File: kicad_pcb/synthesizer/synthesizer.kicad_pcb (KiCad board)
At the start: 2 copper layers, 122.2 x 82 mm, 39 parts, among them J1 RJ45, J5 CONSMA006.062-G, Q1 BCW31_

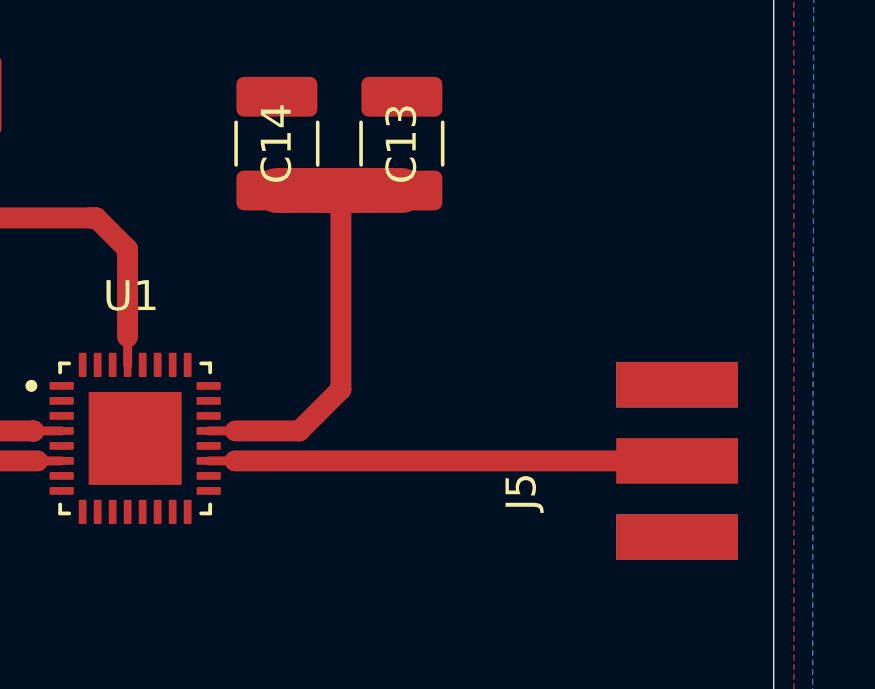
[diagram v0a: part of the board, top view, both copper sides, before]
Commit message: Agregada LineaPCB
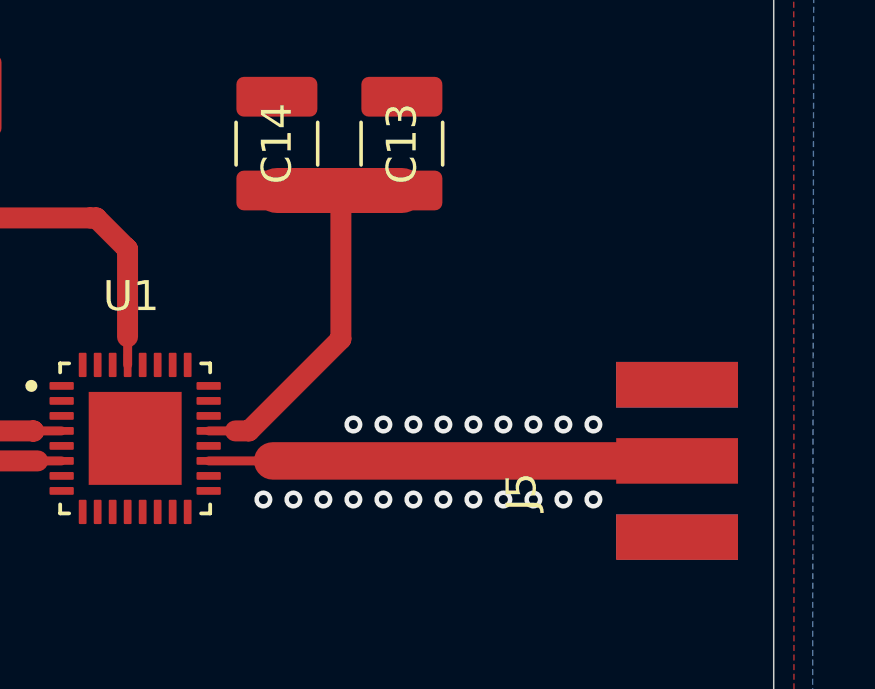
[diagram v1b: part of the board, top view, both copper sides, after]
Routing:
- net +5V: track 127.2 -> 126.3 mm
- net GND: vias 0 -> 21
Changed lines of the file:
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@@
 			(keep_text_aligned yes)
 		)
-		(gr_text "122.2248"
+		(gr_text "122,2248"
 			(at 153.8986 57.9558 0)
 			(layer "Dwgs.User")
@@
 			(keep_text_aligned yes)
 		)
-		(gr_text "82.042"
+		(gr_text "82,042"
 			(at 86.607 105.283 90)
 			(layer "Dwgs.User")
@@
 		(net 2)
 	)
+	(via
+		(at 203 105.5)
+		(size 0.6)
+		(drill 0.3)
+		(layers "F.Cu" "B.Cu")
+		(free yes)
+		(net 2)
+	)
+	(via
+		(at 204 103)
+		(size 0.6)
+		(drill 0.3)
+		(layers "F.Cu" "B.Cu")
+		(free yes)
+		(net 2)
+	)
+	(via
+		(at 209 105.5)
+		(size 0.6)
+		(drill 0.3)
+		(layers "F.Cu" "B.Cu")
+		(free yes)
+		(net 2)
+	)
+	(via
+		(at 209 103)
+		(size 0.6)
+		(drill 0.3)
+		(layers "F.Cu" "B.Cu")
+		(free yes)
+		(net 2)
+	)
+	(via
+		(at 206 103)
+		(size 0.6)
+		(drill 0.3)
+		(layers "F.Cu" "B.Cu")
+		(free yes)
+		(net 2)
+	)
+	(via
+		(at 207 105.5)
+		(size 0.6)
+		(drill 0.3)
+		(layers "F.Cu" "B.Cu")
+		(free yes)
+		(net 2)
+	)
+	(via
+		(at 199 105.5)
+		(size 0.6)
+		(drill 0.3)
+		(layers "F.Cu" "B.Cu")
+		(free yes)
+		(net 2)
+	)
+	(via
+		(at 202 103)
+		(size 0.6)
+		(drill 0.3)
+		(layers "F.Cu" "B.Cu")
+		(free yes)
+		(net 2)
+	)
+	(via
+		(at 198 105.5)
+		(size 0.6)
+		(drill 0.3)
+		(layers "F.Cu" "B.Cu")
+		(free yes)
+		(net 2)
+	)
+	(via
+		(at 208 103)
+		(size 0.6)
+		(drill 0.3)
+		(layers "F.Cu" "B.Cu")
+		(free yes)
+		(net 2)
+	)
+	(via
+		(at 201 103)
+		(size 0.6)
+		(drill 0.3)
+		(layers "F.Cu" "B.Cu")
+		(free yes)
+		(net 2)
+	)
+	(via
+		(at 203 103)
+		(size 0.6)
+		(drill 0.3)
+		(layers "F.Cu" "B.Cu")
+		(free yes)
+		(net 2)
+	)
+	(via
+		(at 201 105.5)
+		(size 0.6)
+		(drill 0.3)
+		(layers "F.Cu" "B.Cu")
+		(free yes)
+		(net 2)
+	)
+	(via
+		(at 202 105.5)
+		(size 0.6)
+		(drill 0.3)
+		(layers "F.Cu" "B.Cu")
+		(free yes)
+		(net 2)
+	)
+	(via
+		(at 205 103)
+		(size 0.6)
+		(drill 0.3)
+		(layers "F.Cu" "B.Cu")
+		(free yes)
+		(net 2)
+	)
+	(via
+		(at 208 105.5)
+		(size 0.6)
+		(drill 0.3)
+		(layers "F.Cu" "B.Cu")
+		(free yes)
+		(net 2)
+	)
+	(via
+		(at 207 103)
+		(size 0.6)
+		(drill 0.3)
+		(layers "F.Cu" "B.Cu")
+		(free yes)
+		(net 2)
+	)
+	(via
+		(at 200 105.5)
+		(size 0.6)
+		(drill 0.3)
+		(layers "F.Cu" "B.Cu")
+		(free yes)
+		(net 2)
+	)
+	(via
+		(at 205 105.5)
+		(size 0.6)
+		(drill 0.3)
+		(layers "F.Cu" "B.Cu")
+		(free yes)
+		(net 2)
+	)
+	(via
+		(at 206 105.5)
+		(size 0.6)
+		(drill 0.3)
+		(layers "F.Cu" "B.Cu")
+		(free yes)
+		(net 2)
+	)
+	(via
+		(at 204 105.5)
+		(size 0.6)
+		(drill 0.3)
+		(layers "F.Cu" "B.Cu")
+		(free yes)
+		(net 2)
+	)
 	(segment
 		(start 190.4779 104.2129)
@@
 	)
 	(segment
+		(start 197.0659 103.2129)
+		(end 197.52 103.2129)
+		(width 0.700001)
+		(layer "F.Cu")
+		(net 3)
+	)
+	(segment
+		(start 197.52 103.2129)
+		(end 200.5838 100.1491)
+		(width 0.700001)
+		(layer "F.Cu")
+		(net 3)
+	)
+	(segment
 		(start 185.7502 114.9604)
 		(end 178.689 114.9604)
@@
 		(end 155.6258 104.9274)
 		(width 0.399999)
-		(layer "F.Cu")
-		(net 3)
-	)
-	(segment
-		(start 200.5838 101.8286)
-		(end 200.5838 95.1992)
-		(width 0.700001)
 		(layer "F.Cu")
 		(net 3)
@@
 	)
 	(segment
-		(start 197.0659 103.2129)
-		(end 199.1995 103.2129)
-		(width 0.700001)
-		(layer "F.Cu")
-		(net 3)
-	)
-	(segment
 		(start 137.9982 108.7751)
 		(end 132.2629 108.7751)
@@
 	)
 	(segment
-		(start 199.1995 103.2129)
-		(end 200.5838 101.8286)
-		(width 0.700001)
-		(layer "F.Cu")
-		(net 3)
-	)
-	(segment
 		(start 128.6256 112.4124)
 		(end 128.3556 112.4124)
 		(width 2.000001)
+		(layer "F.Cu")
+		(net 3)
+	)
+	(segment
+		(start 200.5838 100.1491)
+		(end 200.5838 95.1992)
+		(width 0.700001)
 		(layer "F.Cu")
 		(net 3)
@@
 	)
 	(segment
-		(start 197.0499 104.2129)
+		(start 198.31 104.2129)
+		(end 196.1758 104.2129)
+		(width 0.299999)
+		(layer "F.Cu")
+		(net 19)
+	)
+	(segment
+		(start 198.31 104.2129)
 		(end 211.7902 104.2129)
-		(width 0.700001)
-		(layer "F.Cu")
-		(net 19)
-	)
-	(segment
-		(start 196.1758 104.2129)
-		(end 197.0499 104.2129)
-		(width 0.299999)
+		(width 1.25)
 		(layer "F.Cu")
 		(net 19)
@@
 		(net_name "GND")
 		(layer "F.Cu")
-		(hatch edge 0.5)
-		(connect_pads
-			(clearance 0.5)
+		(hatch edge 0.2)
+		(connect_pads yes
+			(clearance 0.2)
 		)
 		(min_thickness 0.25)

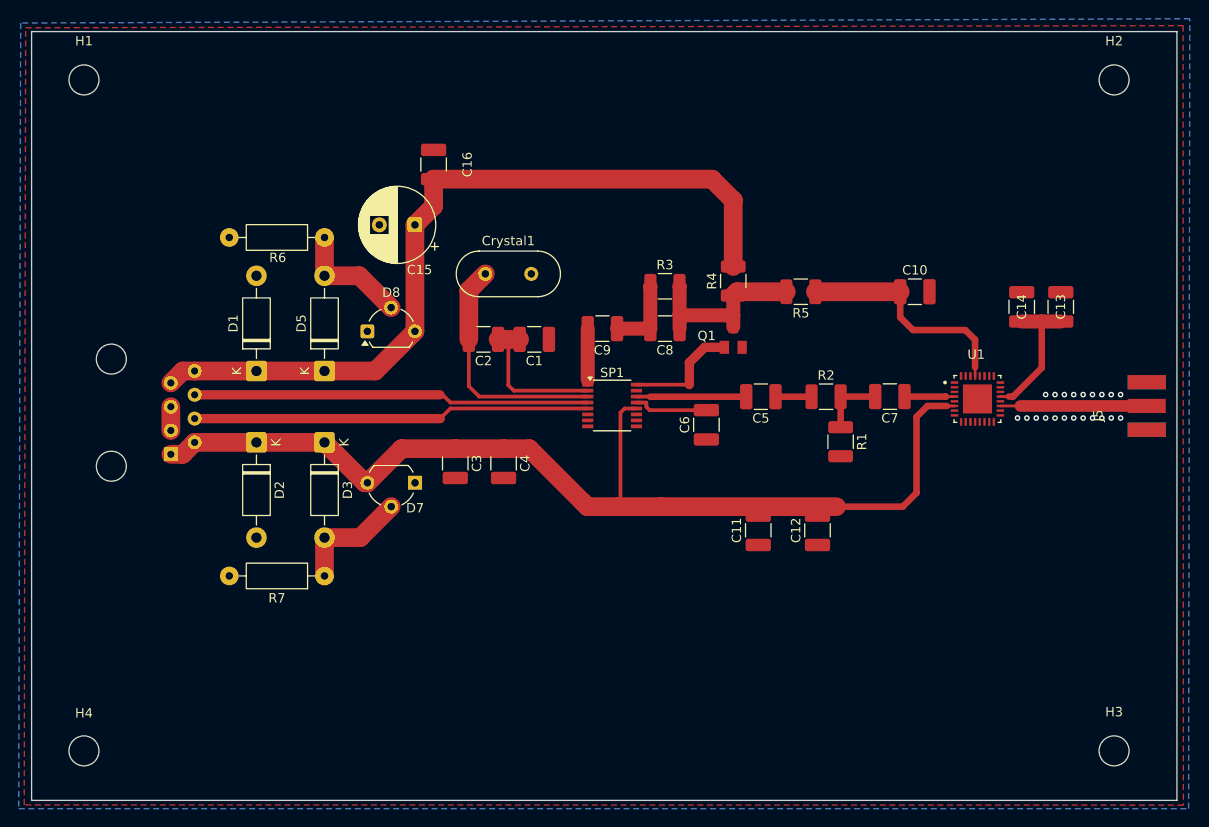
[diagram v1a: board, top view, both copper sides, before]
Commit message: modificación de pcb y esquema
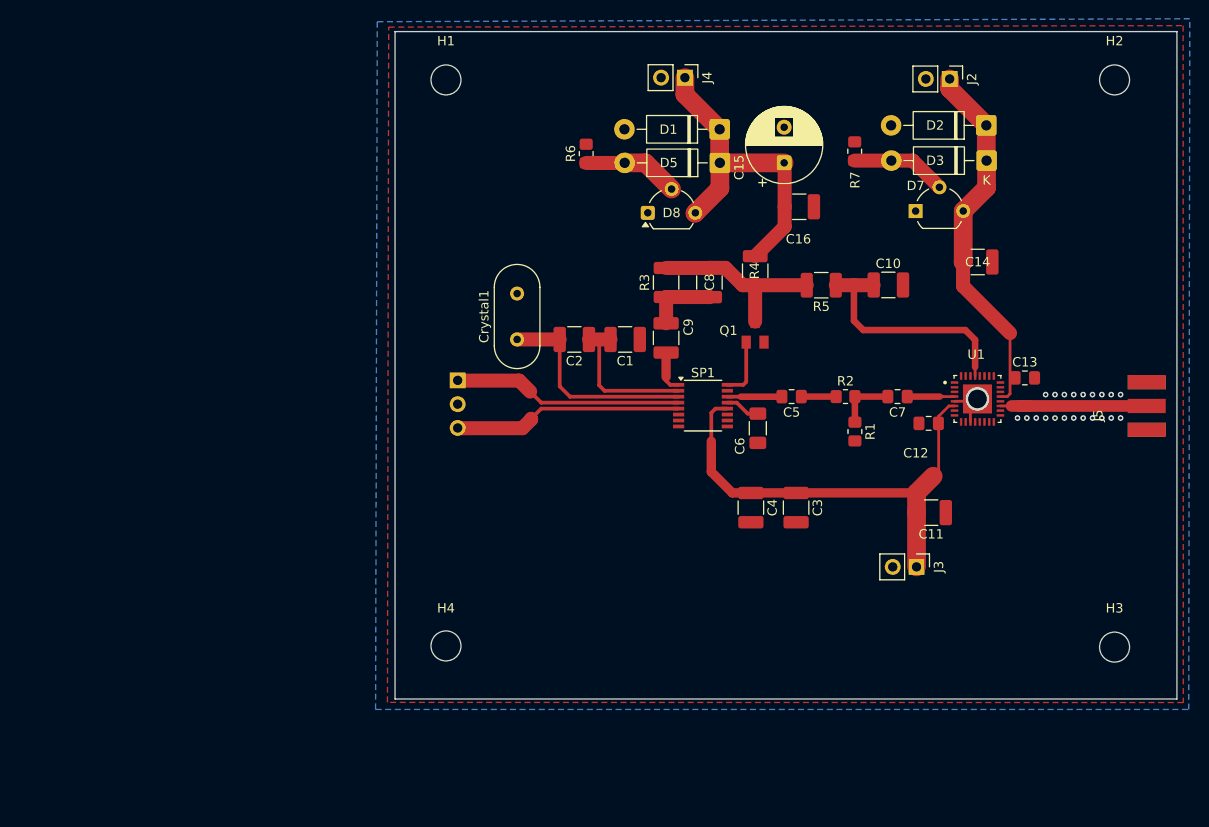
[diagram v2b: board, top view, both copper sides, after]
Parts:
- added J2: Fuente5V, Connector_PinHeader_2.54mm:PinHeader_1x02_P2.54mm_Vertical, F.Cu at (190.8, 69.3)
- added J3: Fuente5V, Connector_PinHeader_2.54mm:PinHeader_1x02_P2.54mm_Vertical, F.Cu at (187.2, 121.4)
- added J4: Fuente12V, Connector_PinHeader_2.54mm:PinHeader_1x02_P2.54mm_Vertical, F.Cu at (162.5, 69.2)
- C12, C13, C5, C7: footprint Capacitor_SMD:C_1210_3225Metric_Pad1.33x2.70mm_HandSolder -> Capacitor_SMD:C_0805_2012Metric_Pad1.18x1.45mm_HandSolder
- C6: footprint Capacitor_SMD:C_1210_3225Metric_Pad1.33x2.70mm_HandSolder -> Capacitor_SMD:C_1206_3216Metric_Pad1.33x1.80mm_HandSolder
- J1: value RJ45 -> SCL_GND_SCA; footprint Connector_RJ:RJ45_Amphenol_54602-x08_Horizontal -> Connector_PinHeader_2.54mm:PinHeader_1x03_P2.54mm_Vertical
- R1, R2: footprint Resistor_SMD:R_1210_3225Metric_Pad1.30x2.65mm_HandSolder -> Resistor_SMD:R_0805_2012Metric_Pad1.20x1.40mm_HandSolder
- R6, R7: footprint Resistor_THT:R_Axial_DIN0207_L6.3mm_D2.5mm_P10.16mm_Horizontal -> Resistor_SMD:R_0805_2012Metric_Pad1.20x1.40mm_HandSolder
- moved D2 84.9 mm to (194.7, 74.3), turned to 180 degrees
- moved D3 76.8 mm to (194.7, 78.0), turned to 180 degrees
- moved R7 72.5 mm to (180.6, 77.0), turned to 90 degrees
- moved D7 60.8 mm to (187.1, 83.4), turned to 0 degrees
- moved D1 55.8 mm to (166.2, 74.7), turned to 180 degrees
- moved D5 47.7 mm to (166.2, 78.3), turned to 180 degrees
- moved H4 40.2 mm to (137.0, 129.9)
- moved C15 40.0 mm to (173.1, 78.3), turned to 90 degrees
- moved C16 39.3 mm to (174.7, 83.0), turned to 0 degrees
- moved H1 38.6 mm to (137.0, 69.4)
- moved C3 36.7 mm to (174.4, 115.1)
- moved D8 32.5 mm to (158.5, 83.6)
- moved J1 31.6 mm to (138.3, 101.5), turned to 180 degrees
- moved R6 29.3 mm to (152.0, 77.3), turned to 90 degrees
- moved C4 26.8 mm to (169.5, 115.1)
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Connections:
- J1 pad 1: +5V -> Net-(J1-Pin_1)
- J1 pad 2: +5V -> GND
- J1 pad 3: GND -> Net-(J1-Pin_3)
- SP1 pad 4: Net-(SP1-SDA) -> Net-(J1-Pin_1)
- SP1 pad 5: Net-(SP1-SCL) -> Net-(J1-Pin_3)
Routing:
- net +12V: track 85.4 -> 35.3 mm
- net Net-(SP1-SCL): track 42.4 -> 0.00 mm
- net Net-(SP1-SDA): track 42.3 -> 0.00 mm
- net +5V: track 126.3 -> 90.0 mm
- net Net-(J1-Pin_1): track 0.00 -> 24.6 mm
- net Net-(J1-Pin_3): track 0.00 -> 24.5 mm
- net Net-(SP1-Drive): track 12.4 -> 6.38 mm
- net Net-(C5-Pad2): track 11.7 -> 5.82 mm
- net Net-(C6-Pad2): track 8.04 -> 3.74 mm
- net Net-(SP1-Crystal): track 25.9 -> 22.7 mm
- net GND: track 2.54 -> 5.31 mm, vias 21 -> 22
- net Net-(D3-A): track 12.6 -> 10.2 mm
- net Net-(D5-A): track 12.6 -> 10.3 mm
- net Net-(U1-RFOUT): track 15.6 -> 17.4 mm
- net Net-(SP1-Charge_Pump): track 5.47 -> 4.52 mm
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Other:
- board size 122.2 x 82 mm -> 83.4 x 71.2 mm

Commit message: Agregadas vias (sin check)
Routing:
- net GND: vias 22 -> 76

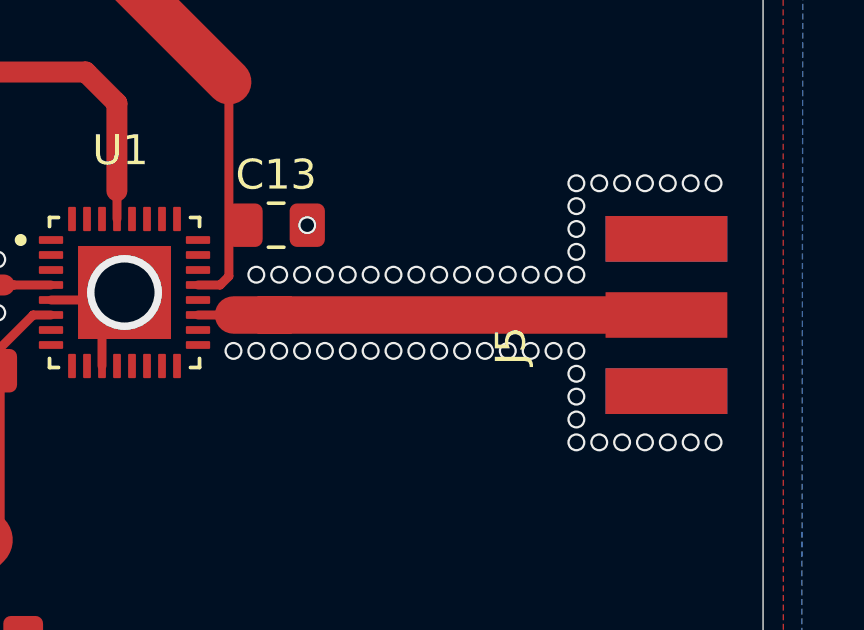
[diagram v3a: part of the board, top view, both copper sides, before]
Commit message: Simulacion pcb
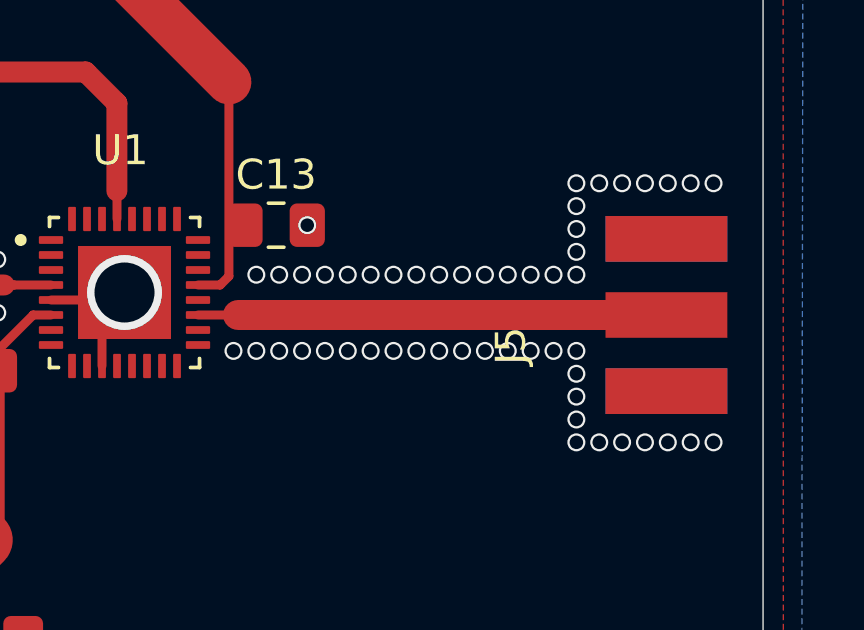
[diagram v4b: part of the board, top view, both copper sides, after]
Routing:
- net Net-(U1-RFOUT): track 17.4 -> 16.4 mm
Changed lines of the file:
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@@
 	)
 	(segment
-		(start 199.136 104.2129)
-		(end 197.360804 104.2129)
-		(width 1.25)
+		(start 197.51 104.2129)
+		(end 211.7902 104.2129)
+		(width 1)
 		(layer "F.Cu")
 		(net 17)
@@
 		(end 196.1758 104.2129)
 		(width 0.299999)
-		(layer "F.Cu")
-		(net 17)
-	)
-	(segment
-		(start 198.31 104.2129)
-		(end 199.136 104.2129)
-		(width 1.25)
-		(layer "F.Cu")
-		(net 17)
-	)
-	(segment
-		(start 199.136 104.2129)
-		(end 211.7902 104.2129)
-		(width 1.25)
 		(layer "F.Cu")
 		(net 17)
@@
 			(clearance 0.2)
 		)
-		(min_thickness 0.25)
+		(min_thickness 0.2)
 		(filled_areas_thickness no)
 		(fill yes

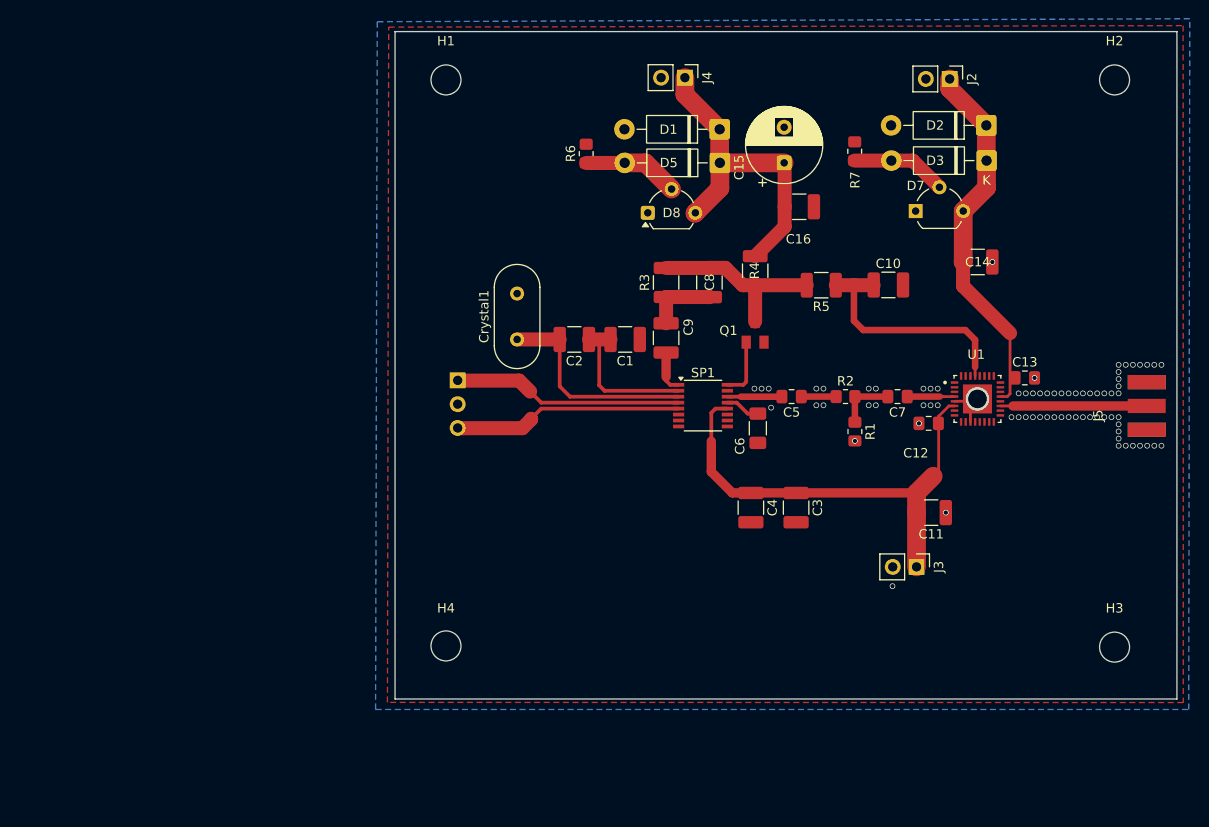
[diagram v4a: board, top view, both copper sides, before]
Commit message: cambio de huella y posiciones de elemenntos. se reduce el tamaño de placa
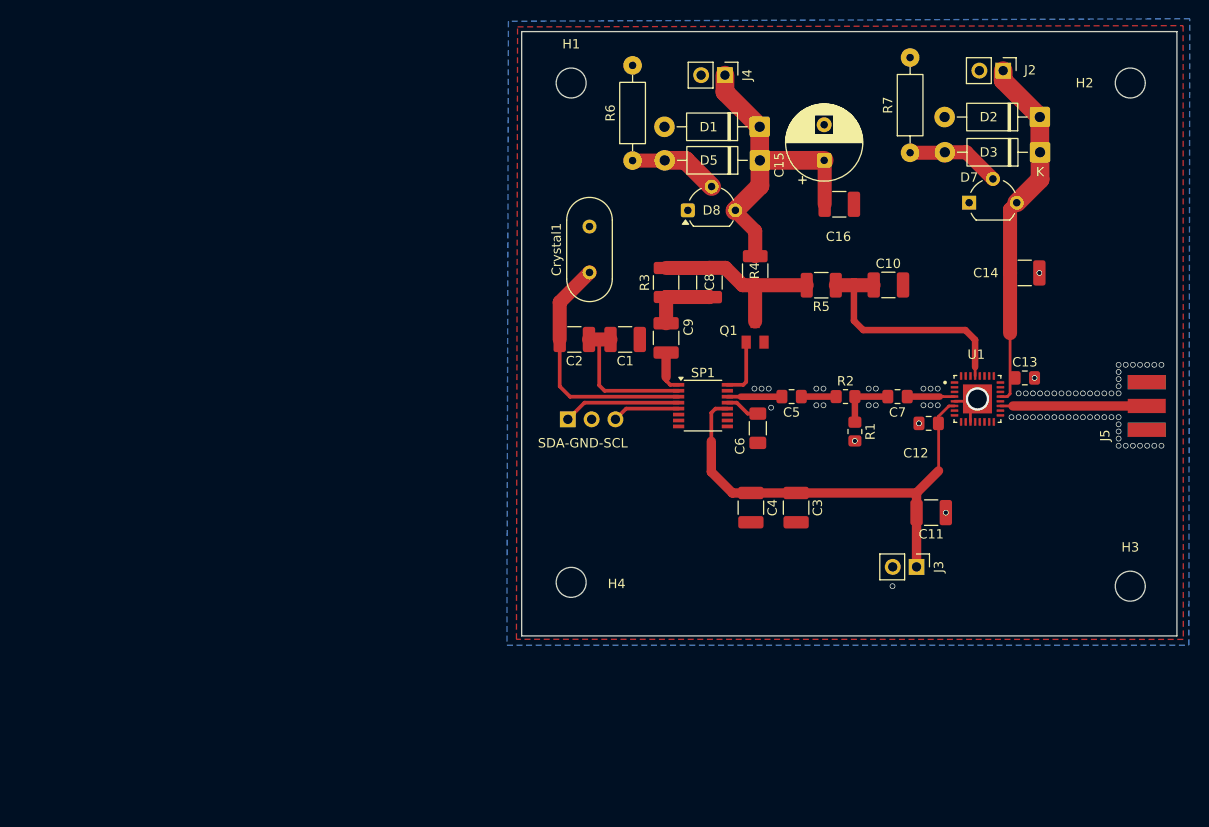
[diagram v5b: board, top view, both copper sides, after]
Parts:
- R6, R7: footprint Resistor_SMD:R_0805_2012Metric_Pad1.20x1.40mm_HandSolder -> Resistor_THT:R_Axial_DIN0207_L6.3mm_D2.5mm_P10.16mm_Horizontal
- moved H4 15.0 mm to (150.4, 123.2)
- moved H1 13.4 mm to (150.4, 69.7)
- moved J1 12.5 mm to (150.0, 105.6), turned to -90 degrees
- moved Crystal1 10.5 mm to (152.3, 90.0)
- moved H3 6.72 mm to (210.0, 123.4)
- moved R7 5.92 mm to (186.5, 77.2)
- moved D3 5.78 mm to (200.4, 77.1)
- moved D7 5.78 mm to (192.8, 82.5)
- moved D2 5.78 mm to (200.4, 73.4)
- moved J2 5.78 mm to (196.5, 68.4)
- moved C14 5.15 mm to (198.8, 90.0)
- moved R6 5.01 mm to (156.9, 78.0)
- moved C15 4.28 mm to (177.4, 78.0)
- moved C16 4.28 mm to (179.0, 82.7)
- moved D1 4.28 mm to (170.5, 74.4)
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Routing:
- net Net-(J1-Pin_3): track 24.5 -> 7.22 mm
- net Net-(J1-Pin_1): track 24.6 -> 12.6 mm
- net Net-(SP1-Crystal): track 22.7 -> 26.6 mm
- net +12V: track 35.3 -> 34.4 mm
- net Net-(D5-A): track 10.3 -> 9.60 mm
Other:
- board size 83.4 x 71.2 mm -> 69.9 x 64.5 mm
- board text added: "SDA-GND-SCL"

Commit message: Se agregan caps para sda y scl
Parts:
- added C17: 100p, Capacitor_SMD:C_1210_3225Metric_Pad1.33x2.70mm_HandSolder, F.Cu at (150.0, 111.7)
- added C18: 100p, Capacitor_SMD:C_1210_3225Metric_Pad1.33x2.70mm_HandSolder, F.Cu at (155.1, 111.7)
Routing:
- net Net-(J1-Pin_1): track 12.6 -> 17.1 mm
- net Net-(J1-Pin_3): track 7.22 -> 11.7 mm
